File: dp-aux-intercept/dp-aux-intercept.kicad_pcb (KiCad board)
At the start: 2 copper layers, 24 parts

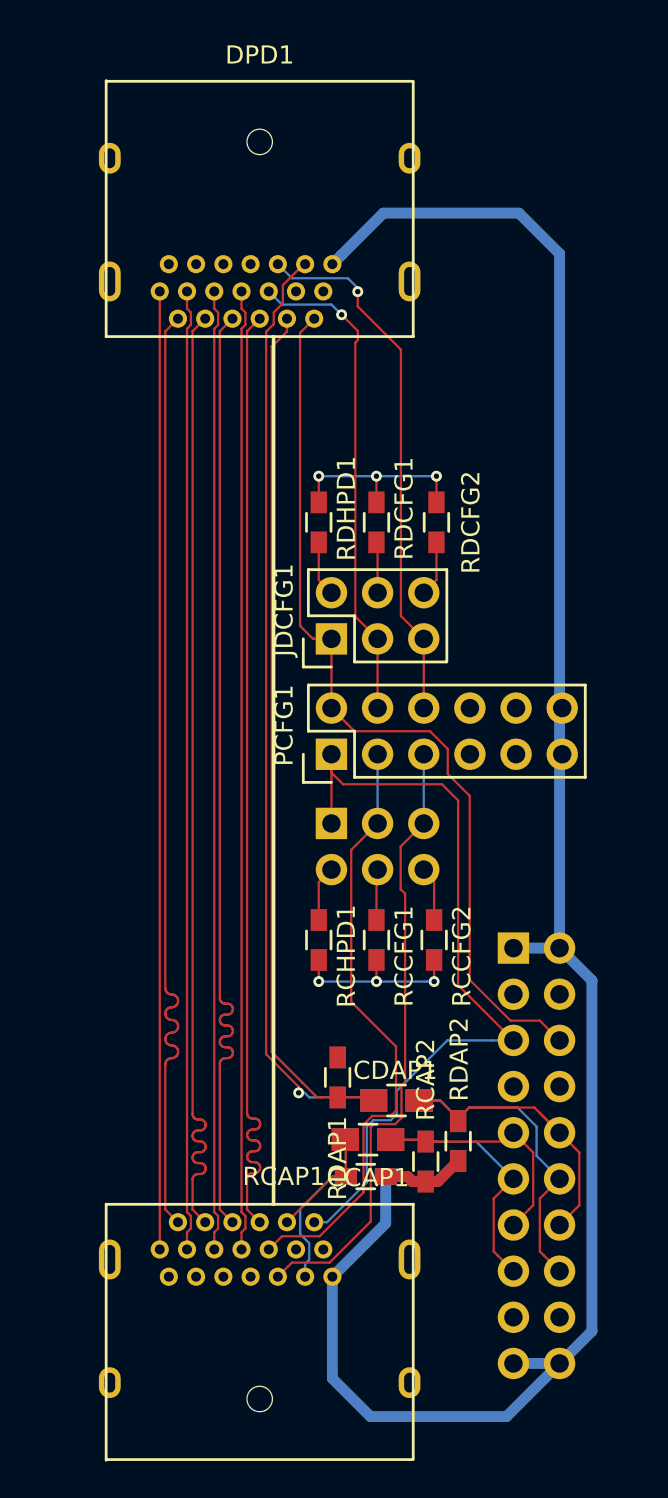
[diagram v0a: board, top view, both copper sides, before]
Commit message: Fixing the vias
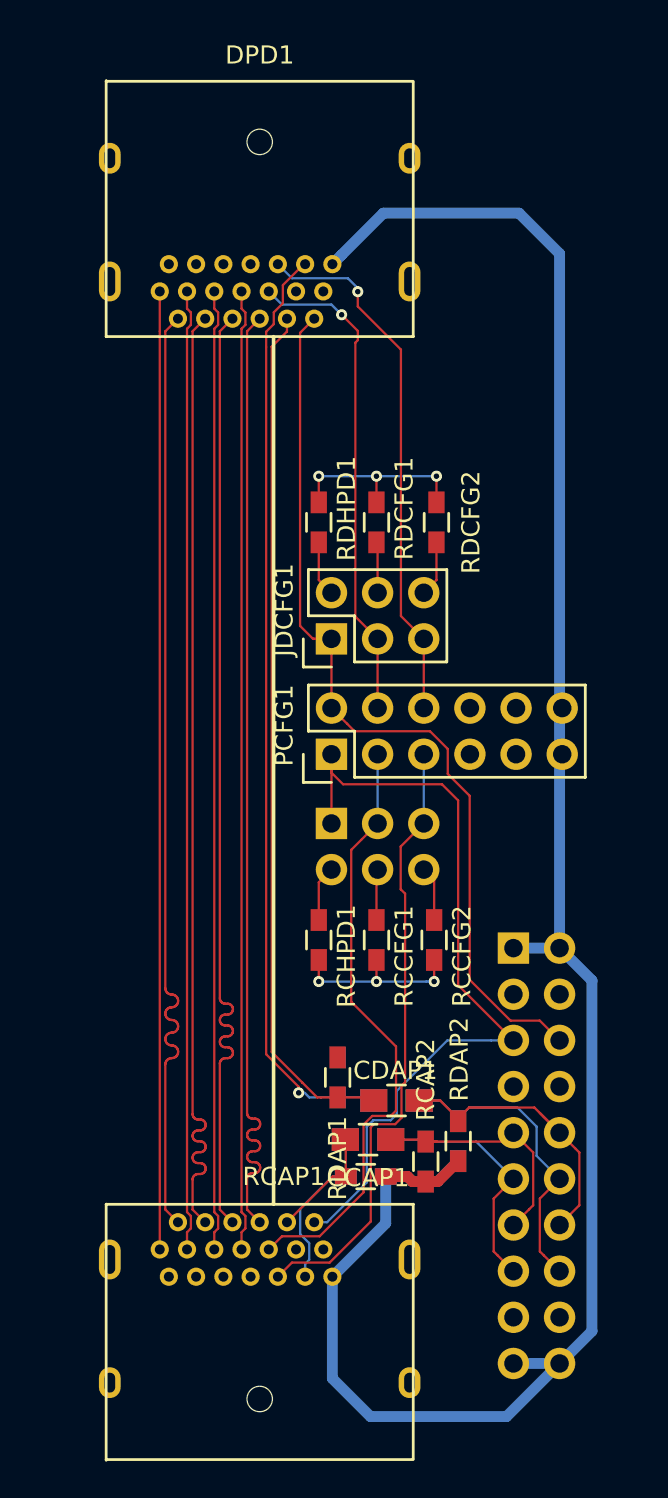
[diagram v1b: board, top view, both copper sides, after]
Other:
- net class Default: via_dia 0.6 -> 0.6096; via_drill 0.3 -> 0.3048
- net class VDD: trace_width 0.6 -> 0.6096; via_dia 0.6 -> 0.6096; via_drill 0.3 -> 0.3048
- rule via_min_drill: 0.3 -> 0.3048
- rule via_min_size: 0.6 -> 0.6096
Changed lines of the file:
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@@
     (last_trace_width 0.127)
-    (user_trace_width 0.127)
     (user_trace_width 0.127)
     (trace_clearance 0.127)
@@
     (segment_width 0.2)
     (edge_width 0.1)
-    (via_size 0.6)
-    (via_drill 0.3)
-    (via_min_size 0.6)
-    (via_min_drill 0.3)
+    (via_size 0.6096)
+    (via_drill 0.3048)
+    (via_min_size 0.6096)
+    (via_min_drill 0.3048)
+    (user_via 0.6096 0.3048)
     (uvia_size 0.3)
     (uvia_drill 0.1)
@@
     (clearance 0.127)
     (trace_width 0.127)
-    (via_dia 0.6)
-    (via_drill 0.3)
+    (via_dia 0.6096)
+    (via_drill 0.3048)
     (uvia_dia 0.3)
     (uvia_drill 0.1)
@@
   (net_class VDD ""
     (clearance 0.127)
-    (trace_width 0.6)
-    (via_dia 0.6)
-    (via_drill 0.3)
+    (trace_width 0.6096)
+    (via_dia 0.6096)
+    (via_drill 0.3048)
     (uvia_dia 0.3)
     (uvia_drill 0.1)
@@
   (segment (start 32.467001 33.035001) (end 35.194001 33.035001) (width 0.127) (layer B.Cu) (net 4))
   (segment (start 35.194001 33.035001) (end 35.7505 33.5915) (width 0.127) (layer B.Cu) (net 4))
-  (via (at 35.7505 33.5915) (size 0.6) (drill 0.3) (layers F.Cu B.Cu) (net 4))
+  (via (at 35.7505 33.5915) (size 0.6096) (drill 0.3048) (layers F.Cu B.Cu) (net 4))
   (segment (start 37.7317 55.24246) (end 37.7317 54.021146) (width 0.127) (layer F.Cu) (net 4))
   (segment (start 37.7317 54.021146) (end 37.7317 51.43246) (width 0.127) (layer F.Cu) (net 4))
@@
   (segment (start 39.0144 50.17516) (end 40.2717 51.43246) (width 0.127) (layer F.Cu) (net 5))
   (segment (start 36.6395 32.131) (end 36.6395 32.3215) (width 0.127) (layer B.Cu) (net 5))
-  (via (at 36.6395 32.3215) (size 0.6) (drill 0.3) (layers F.Cu B.Cu) (net 5))
+  (via (at 36.6395 32.3215) (size 0.6096) (drill 0.3048) (layers F.Cu B.Cu) (net 5))
   (segment (start 36.093499 31.584999) (end 36.6395 32.131) (width 0.127) (layer B.Cu) (net 5))
   (segment (start 32.242 30.81) (end 33.016999 31.584999) (width 0.127) (layer B.Cu) (net 5))
@@
   (segment (start 35.1917 55.24246) (end 35.1917 51.43246) (width 0.127) (layer F.Cu) (net 6))
   (segment (start 37.6682 43.91896) (end 37.6682 42.47896) (width 0.127) (layer F.Cu) (net 7))
-  (via (at 37.6682 42.47896) (size 0.6) (drill 0.3) (layers F.Cu B.Cu) (net 7))
+  (via (at 37.6682 42.47896) (size 0.6096) (drill 0.3048) (layers F.Cu B.Cu) (net 7))
   (segment (start 40.9702 42.47896) (end 40.9702 43.91896) (width 0.127) (layer F.Cu) (net 7))
   (segment (start 34.4932 42.47896) (end 40.9702 42.47896) (width 0.127) (layer B.Cu) (net 7))
-  (via (at 40.9702 42.47896) (size 0.6) (drill 0.3) (layers F.Cu B.Cu) (net 7))
+  (via (at 40.9702 42.47896) (size 0.6096) (drill 0.3048) (layers F.Cu B.Cu) (net 7))
   (segment (start 34.4932 43.91896) (end 34.4932 42.47896) (width 0.127) (layer F.Cu) (net 7))
-  (via (at 34.4932 42.47896) (size 0.6) (drill 0.3) (layers F.Cu B.Cu) (net 7))
+  (via (at 34.4932 42.47896) (size 0.6096) (drill 0.3048) (layers F.Cu B.Cu) (net 7))
   (segment (start 37.6682 69.10596) (end 37.6682 70.29196) (width 0.127) (layer F.Cu) (net 7))
-  (via (at 37.6682 70.29196) (size 0.6) (drill 0.3) (layers F.Cu B.Cu) (net 7))
+  (via (at 37.6682 70.29196) (size 0.6096) (drill 0.3048) (layers F.Cu B.Cu) (net 7))
   (segment (start 34.4932 70.29196) (end 34.4932 69.10596) (width 0.127) (layer F.Cu) (net 7))
   (segment (start 40.418936 70.29196) (end 34.4932 70.29196) (width 0.127) (layer B.Cu) (net 7))
-  (via (at 34.4932 70.29196) (size 0.6) (drill 0.3) (layers F.Cu B.Cu) (net 7))
+  (via (at 34.4932 70.29196) (size 0.6096) (drill 0.3048) (layers F.Cu B.Cu) (net 7))
   (segment (start 40.8432 70.29196) (end 40.418936 70.29196) (width 0.127) (layer B.Cu) (net 7))
   (segment (start 40.8432 69.10596) (end 40.8432 70.29196) (width 0.127) (layer F.Cu) (net 7))
-  (via (at 40.8432 70.29196) (size 0.6) (drill 0.3) (layers F.Cu B.Cu) (net 7))
+  (via (at 40.8432 70.29196) (size 0.6096) (drill 0.3048) (layers F.Cu B.Cu) (net 7))
   (segment (start 47.74692 68.453) (end 47.74692 30.23108) (width 0.6) (layer B.Cu) (net 8))
   (segment (start 47.74692 30.23108) (end 45.51934 28.0035) (width 0.6) (layer B.Cu) (net 8))
@@
   (segment (start 34.625678 76.67008) (end 35.53206 76.67008) (width 0.127) (layer B.Cu) (net 20))
   (segment (start 33.385579 76.082746) (end 33.385579 76.418621) (width 0.127) (layer F.Cu) (net 20))
-  (via (at 33.385579 76.418621) (size 0.6) (drill 0.3) (layers F.Cu B.Cu) (net 20))
+  (via (at 33.385579 76.418621) (size 0.6096) (drill 0.3048) (layers F.Cu B.Cu) (net 20))
   (segment (start 31.5975 74.294667) (end 33.385579 76.082746) (width 0.127) (layer F.Cu) (net 20))
   (segment (start 31.5975 35.369834) (end 31.5975 74.294667) (width 0.127) (layer F.Cu) (net 20))

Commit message: Adding ground plane and tie vias
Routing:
- net GND: vias 6 -> 168
- added copper zone on B.Cu, net GND
- added copper zone on F.Cu, net GND
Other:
- board outline added: 29.7 x 72.8 mm

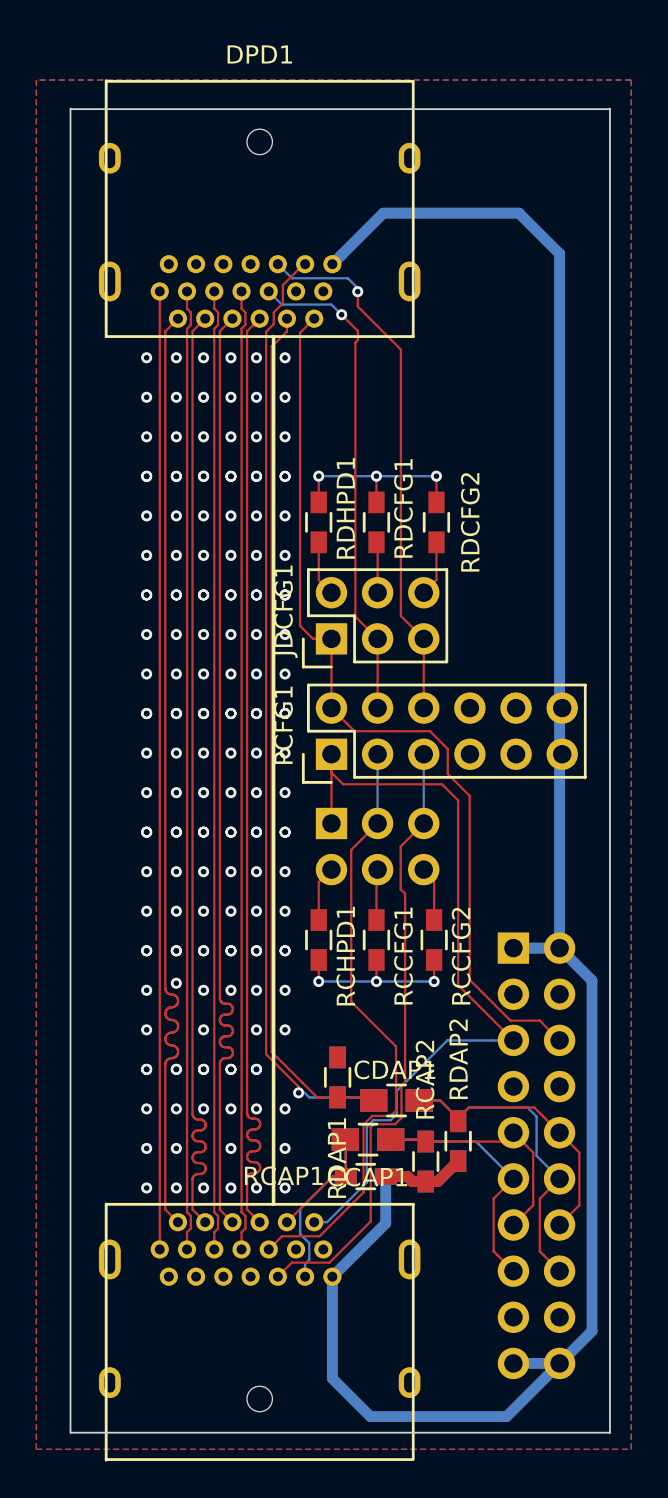
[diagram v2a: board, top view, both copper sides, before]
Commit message: Lots of work.
 * Fixing the GND tie vias.
 * Working on the silkscreen.
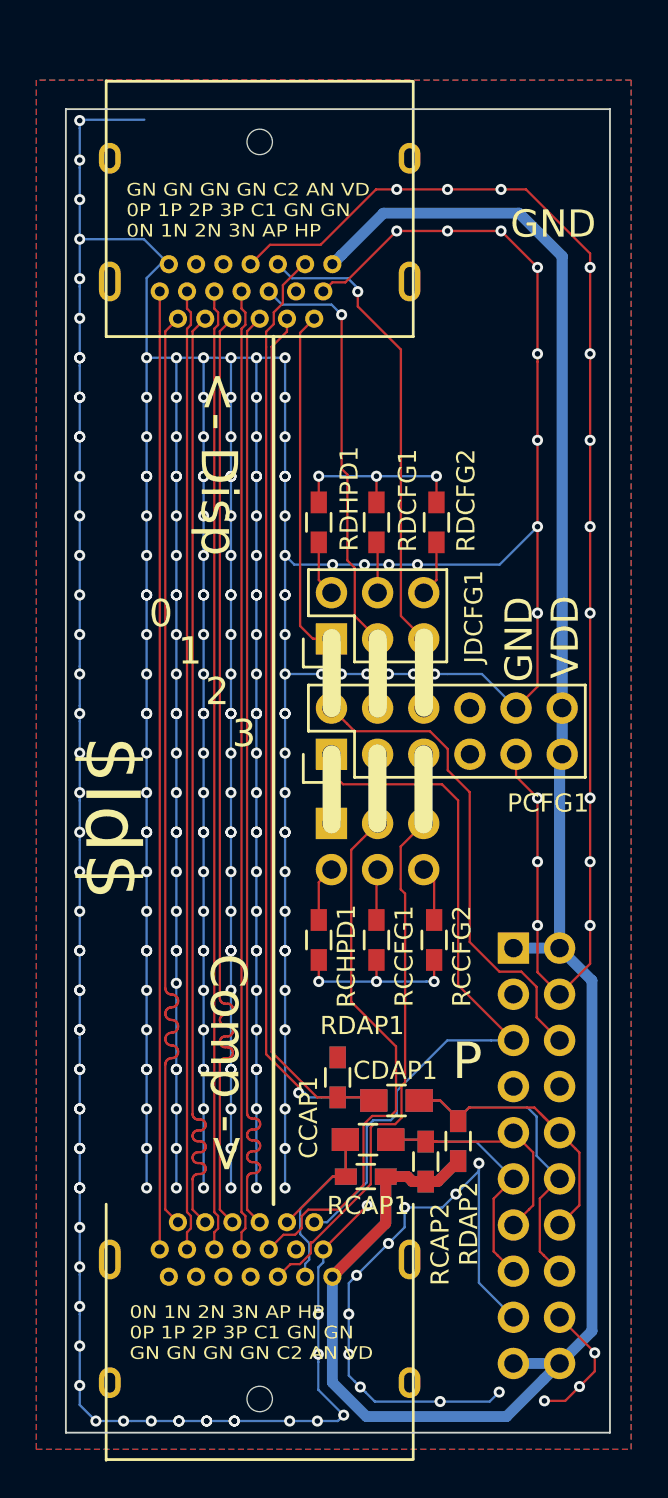
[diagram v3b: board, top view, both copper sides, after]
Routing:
- net GND: track 20.7 -> 602.5 mm, vias 168 -> 271
- net VDD: track 118.3 -> 125.3 mm
- net /CCFG2: track 34.2 -> 33.3 mm
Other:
- board size 29.7 x 72.8 mm -> 29.9 x 72.9 mm
- board text added: "$Id$"
- board text added: "0"
- board text added: "0N 1N 2N 3N AP HP 0P 1P 2P 3P C1 GN GN GN GN GN GN C2 AN VD"
- board text added: "1"
- board text added: "2"
- board text added: "3"
- board text added: "<- Disp"
- board text added: "CFG1"
- board text added: "CFG2"
- board text added: "Comp ->"
- board text added: "G"
- board text added: "GN GN GN GN C2 AN VD 0P 1P 2P 3P C1 GN GN 0N 1N 2N 3N AP HP"
- board text added: "GND"
- board text added: "H"
- board text added: "HPD"
- board text added: "N"
- board text added: "P"
- board text added: "V"
- board text added: "VDD"
